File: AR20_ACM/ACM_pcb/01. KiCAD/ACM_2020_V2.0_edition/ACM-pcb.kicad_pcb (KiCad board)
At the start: 2 copper layers, 19.8 x 28 mm, 33 parts, among them J1 TC2030-MCP-NL, P1 Conn_02x15_Odd_Even, Q1 Q_PMOS_DMP3099L-13, U1 ATmega328P-AU, U2 MCP2542FDxMF, U3 NCV890430MW50TXG, U4 MCP2517FD-xSL, Y1 16.0Mhz, Y2 20.0 Mhz

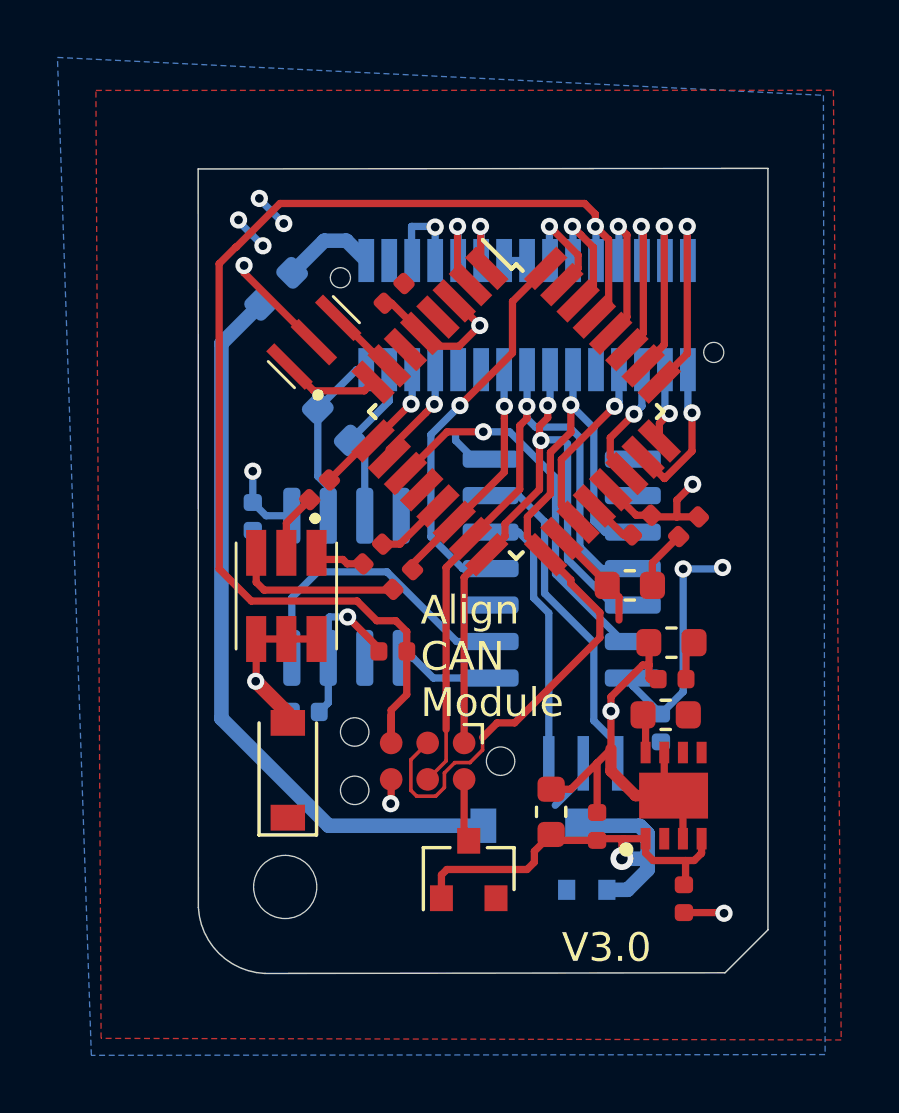
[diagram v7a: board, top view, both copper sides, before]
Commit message: Changed footprint for connector
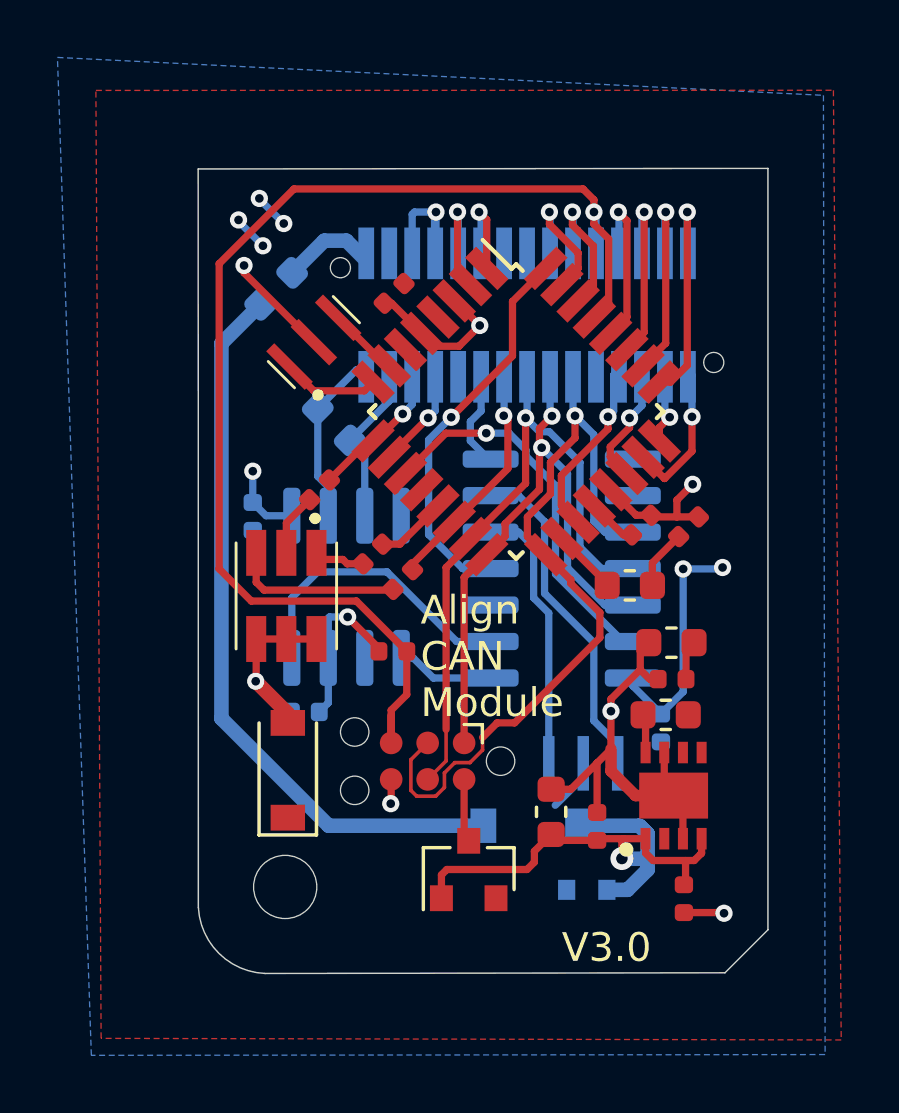
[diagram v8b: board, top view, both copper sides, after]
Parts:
- P1: footprint SMLP36RGB2W3R:ILWX10SBVFBE -> ACM_2020_V2:IL-WX-30SB-VF-BE
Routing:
- net /U-Pin2: track 7.02 -> 8.25 mm
- net /U-Pin20: track 2.75 -> 3.79 mm
- net /U-Pin4: track 6.36 -> 7.38 mm
- net /U-Pin22: track 3.41 -> 4.42 mm
- net /U-Pin6: track 5.75 -> 6.76 mm
- net /U-Pin8: track 5.28 -> 6.28 mm
- net /U-Pin14: track 3.87 -> 4.87 mm
- net /U-Pin12: track 4.31 -> 5.31 mm
- net /MOSI: track 24.2 -> 23.3 mm
- net /Reset: track 42.4 -> 43.2 mm
- net GND: track 42.9 -> 43.5 mm
- net /MISO: track 22.2 -> 21.7 mm
